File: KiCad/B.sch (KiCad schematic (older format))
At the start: 6 parts

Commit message: update schematics and libraries
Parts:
- removed LS?: Speaker, symbol Device:Speaker
- Ra3, Ra4: renamed from Ra?; value R -> R2
- Rb3, Rb4: renamed from Rb?; value R -> R1
- U2: renamed from U?; value LM321 -> U1
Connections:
- net Uout: now reaches Rb4.1, U2.4
- net in renamed Uin
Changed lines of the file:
@@
 $EndDescr
 $Comp
-L Amplifier_Operational:LM321 U?
+L Amplifier_Operational:LM321 U2
 U 1 1 617891E9
 P 5750 3750
-F 0 "U?" H 6094 3796 50  0000 L CNN
-F 1 "LM321" H 6094 3705 50  0001 L CNN
+F 0 "U2" H 6094 3796 50  0001 L CNN
+F 1 "U1" H 5800 3900 50  0000 L CNN
 F 2 "Package_TO_SOT_SMD:SOT-23-5" H 5750 3750 50  0001 C CNN
 F 3 "http://www.ti.com/lit/ds/symlink/lm321.pdf" H 5750 3750 50  0001 C CNN
@@
 	1    0    0    -1
 $EndComp
-$Comp
-L Device:Speaker LS?
-U 1 1 617891EF
-P 6700 3750
-F 0 "LS?" H 6870 3746 50  0000 L CNN
-F 1 "Speaker" H 6870 3655 50  0000 L CNN
-F 2 "" H 6700 3550 50  0001 C CNN
-F 3 "~" H 6690 3700 50  0001 C CNN
-	1    6700 3750
-	1    0    0    -1
-$EndComp
 Wire Wire Line
-	6500 3850 6300 3850
-Wire Wire Line
-	6300 3850 6300 4150
-$Comp
-L power:GND #PWR?
-U 1 1 617891F7
-P 6300 4150
-F 0 "#PWR?" H 6300 3900 50  0001 C CNN
-F 1 "GND" H 6305 3977 50  0000 C CNN
-F 2 "" H 6300 4150 50  0001 C CNN
-F 3 "" H 6300 4150 50  0001 C CNN
-	1    6300 4150
-	1    0    0    -1
-$EndComp
-Wire Wire Line
-	5300 3850 5350 3850
+	5150 3850 5250 3850
 Wire Wire Line
 	5450 3650 5250 3650
-Text GLabel 4900 3850 0    50   Input ~ 0
-in
-$Comp
-L Device:R Ra?
-U 1 1 61789200
-P 4950 3650
-F 0 "Ra?" V 4835 3650 50  0000 C CNN
-F 1 "R" V 4834 3650 50  0001 C CNN
-F 2 "" V 4880 3650 50  0001 C CNN
-F 3 "~" H 4950 3650 50  0001 C CNN
-	1    4950 3650
-	0    1    1    0
-$EndComp
-Wire Wire Line
-	4650 3650 4800 3650
+Text GLabel 4750 3850 0    50   Input ~ 0
+Uin
 Wire Wire Line
 	5250 3650 5250 3450
 Connection ~ 5250 3650
 Wire Wire Line
-	5250 3650 5100 3650
+	5250 3650 5150 3650
 $Comp
-L Device:R Rb?
+L Device:R Rb3
 U 1 1 6178920A
 P 5250 3300
-F 0 "Rb?" H 5320 3300 50  0000 L CNN
-F 1 "R" H 5320 3255 50  0001 L CNN
+F 0 "Rb3" H 5320 3300 50  0001 L CNN
+F 1 "R1" H 5300 3300 50  0000 L CNN
 F 2 "" V 5180 3300 50  0001 C CNN
 F 3 "~" H 5250 3300 50  0001 C CNN
@@
 	5650 3450 5650 3400
 $Comp
-L power:VCC #PWR?
+L power:VCC #PWR06
 U 1 1 61789213
 P 5650 3400
-F 0 "#PWR?" H 5650 3250 50  0001 C CNN
+F 0 "#PWR06" H 5650 3250 50  0001 C CNN
 F 1 "VCC" H 5667 3573 50  0000 C CNN
 F 2 "" H 5650 3400 50  0001 C CNN
@@
 	5650 4050 5650 4100
 $Comp
-L power:GND #PWR?
+L power:GND #PWR07
 U 1 1 6178921A
 P 5650 4100
-F 0 "#PWR?" H 5650 3850 50  0001 C CNN
+F 0 "#PWR07" H 5650 3850 50  0001 C CNN
 F 1 "GND" H 5655 3927 50  0000 C CNN
 F 2 "" H 5650 4100 50  0001 C CNN
@@
 	1    0    0    -1
 $EndComp
-Wire Wire Line
-	4650 3650 4650 3750
 $Comp
-L power:GND #PWR?
+L power:GND #PWR05
 U 1 1 61789221
-P 4650 3750
-F 0 "#PWR?" H 4650 3500 50  0001 C CNN
-F 1 "GND" H 4655 3577 50  0000 C CNN
-F 2 "" H 4650 3750 50  0001 C CNN
-F 3 "" H 4650 3750 50  0001 C CNN
-	1    4650 3750
-	1    0    0    -1
-$EndComp
-Wire Wire Line
-	4900 3850 5000 3850
-$Comp
-L Device:R Ra?
-U 1 1 61789228
-P 5150 3850
-F 0 "Ra?" V 5035 3850 50  0000 C CNN
-F 1 "R" V 5034 3850 50  0001 C CNN
-F 2 "" V 5080 3850 50  0001 C CNN
-F 3 "~" H 5150 3850 50  0001 C CNN
-	1    5150 3850
-	0    1    1    0
-$EndComp
-Connection ~ 5350 3850
-Wire Wire Line
-	5350 3850 5450 3850
-Wire Wire Line
-	5350 4450 5700 4450
-Wire Wire Line
-	5350 3850 5350 4450
-$Comp
-L Device:R Rb?
-U 1 1 61789232
-P 5850 4450
-F 0 "Rb?" V 5735 4450 50  0000 C CNN
-F 1 "R" V 5734 4450 50  0001 C CNN
-F 2 "" V 5780 4450 50  0001 C CNN
-F 3 "~" H 5850 4450 50  0001 C CNN
-	1    5850 4450
+P 4750 3650
+F 0 "#PWR05" H 4750 3400 50  0001 C CNN
+F 1 "GND" H 4755 3477 50  0000 C CNN
+F 2 "" H 4750 3650 50  0001 C CNN
+F 3 "" H 4750 3650 50  0001 C CNN
+	1    4750 3650
 	0    1    1    0
 $EndComp
 Wire Wire Line
-	6000 4450 6200 4450
+	4750 3850 4850 3850
+$Comp
+L Device:R Ra4
+U 1 1 61789228
+P 5000 3850
+F 0 "Ra4" V 4885 3850 50  0001 C CNN
+F 1 "R2" V 5100 3850 50  0000 C CNN
+F 2 "" V 4930 3850 50  0001 C CNN
+F 3 "~" H 5000 3850 50  0001 C CNN
+	1    5000 3850
+	0    1    1    0
+$EndComp
+Connection ~ 5250 3850
 Wire Wire Line
-	6200 4450 6200 3750
-Connection ~ 6200 3750
+	5250 3850 5450 3850
 Wire Wire Line
-	6200 3750 6050 3750
+	5250 4400 5500 4400
 Wire Wire Line
-	6200 3750 6500 3750
+	5250 3850 5250 4400
+$Comp
+L Device:R Rb4
+U 1 1 61789232
+P 5650 4400
+F 0 "Rb4" V 5535 4400 50  0001 C CNN
+F 1 "R1" V 5750 4400 50  0000 C CNN
+F 2 "" V 5580 4400 50  0001 C CNN
+F 3 "~" H 5650 4400 50  0001 C CNN
+	1    5650 4400
+	0    1    1    0
+$EndComp
+Wire Wire Line
+	5800 4400 6100 4400
+Wire Wire Line
+	6100 4400 6100 3750
+Connection ~ 6100 3750
+Wire Wire Line
+	6100 3750 6050 3750
+Wire Wire Line
+	6100 3750 6200 3750
+$Comp
+L Device:R Ra3
+U 1 1 61789200
+P 5000 3650
+F 0 "Ra3" V 4885 3650 50  0001 C CNN
+F 1 "R2" V 4884 3650 50  0000 C CNN
+F 2 "" V 4930 3650 50  0001 C CNN
+F 3 "~" H 5000 3650 50  0001 C CNN
+	1    5000 3650
+	0    1    1    0
+$EndComp
+Wire Wire Line
+	4750 3650 4850 3650
+Text GLabel 6200 3750 2    50   Input ~ 0
+Uout
 $EndSCHEMATC

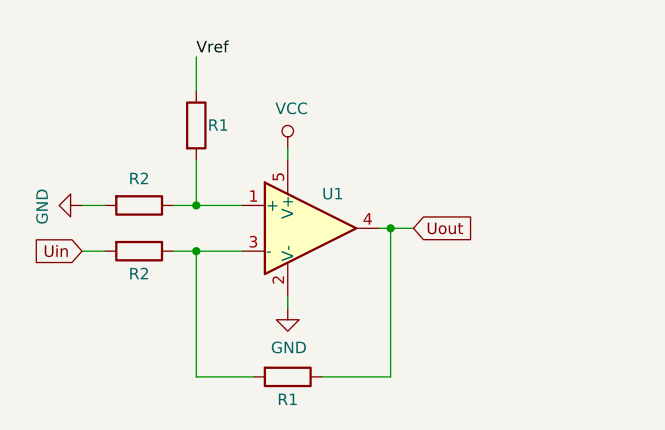
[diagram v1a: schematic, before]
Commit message: corrected opamp circuits
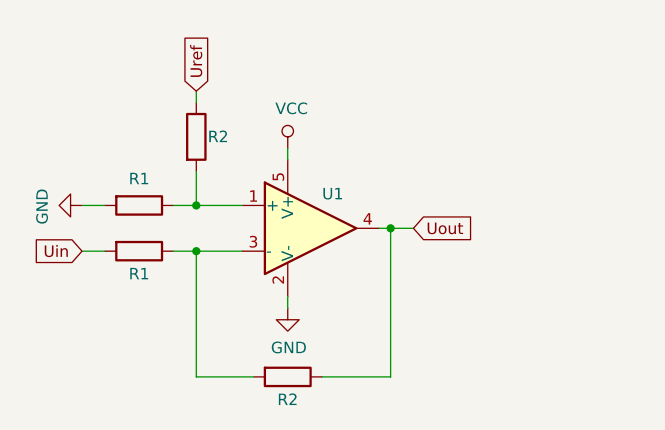
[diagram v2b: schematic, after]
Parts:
- Ra3, Ra4: value R2 -> R1
- Rb3, Rb4: value R1 -> R2
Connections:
- net Vref renamed Uref
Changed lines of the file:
@@
 Uin
 Wire Wire Line
-	5250 3650 5250 3450
+	5250 3650 5250 3500
 Connection ~ 5250 3650
 Wire Wire Line
@@
 L Device:R Rb3
 U 1 1 6178920A
-P 5250 3300
-F 0 "Rb3" H 5320 3300 50  0001 L CNN
-F 1 "R1" H 5300 3300 50  0000 L CNN
-F 2 "" V 5180 3300 50  0001 C CNN
-F 3 "~" H 5250 3300 50  0001 C CNN
-	1    5250 3300
+P 5250 3350
+F 0 "Rb3" H 5320 3350 50  0001 L CNN
+F 1 "R2" H 5300 3350 50  0000 L CNN
+F 2 "" V 5180 3350 50  0001 C CNN
+F 3 "~" H 5250 3350 50  0001 C CNN
+	1    5250 3350
 	1    0    0    -1
 $EndComp
 Wire Wire Line
-	5250 3150 5250 3000
-Text Label 5250 3000 0    50   ~ 0
-Vref
+	5250 3200 5250 3150
 Wire Wire Line
 	5650 3450 5650 3400
@@
 P 5000 3850
 F 0 "Ra4" V 4885 3850 50  0001 C CNN
-F 1 "R2" V 5100 3850 50  0000 C CNN
+F 1 "R1" V 5100 3850 50  0000 C CNN
 F 2 "" V 4930 3850 50  0001 C CNN
 F 3 "~" H 5000 3850 50  0001 C CNN
@@
 P 5650 4400
 F 0 "Rb4" V 5535 4400 50  0001 C CNN
-F 1 "R1" V 5750 4400 50  0000 C CNN
+F 1 "R2" V 5750 4400 50  0000 C CNN
 F 2 "" V 5580 4400 50  0001 C CNN
 F 3 "~" H 5650 4400 50  0001 C CNN
@@
 P 5000 3650
 F 0 "Ra3" V 4885 3650 50  0001 C CNN
-F 1 "R2" V 4884 3650 50  0000 C CNN
+F 1 "R1" V 4884 3650 50  0000 C CNN
 F 2 "" V 4930 3650 50  0001 C CNN
 F 3 "~" H 5000 3650 50  0001 C CNN
@@
 Text GLabel 6200 3750 2    50   Input ~ 0
 Uout
+Text GLabel 5250 3150 1    50   Input ~ 0
+Uref
 $EndSCHEMATC
